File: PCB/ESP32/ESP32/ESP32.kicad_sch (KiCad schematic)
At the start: 32 parts, among them J1 Camera_Receptacle_THT, J1 Conn_01x02_Pin, J1 USB_B_Micro, J2 Conn_01x02_Socket, SW1 RESET, SW2 BOOT, SW3 LRA Switch, U1 DRV2605LTDGSRQ1, U1 ESP32-S2-SOLO-U-N4, U1 MCP73832T-2ACI/OT

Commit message: Footprints for battery
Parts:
- C1, C2: footprint (none) -> Capacitor_SMD:C_0603_1608Metric_Pad1.08x0.95mm_HandSolder
- D1, D2: footprint (none) -> Diode_SMD:D_0603_1608Metric_Pad1.05x0.95mm_HandSolder
- J2: footprint (none) -> Connector_JST:JST_GH_BM02B-GHS-TBT_1x02-1MP_P1.25mm_Vertical
- JP1, JP2: footprint (none) -> Jumper:SolderJumper-2_P1.3mm_Bridged2Bar_Pad1.0x1.5mm
- R1, R2, R3, R4: footprint (none) -> Resistor_SMD:R_0603_1608Metric_Pad0.98x0.95mm_HandSolder
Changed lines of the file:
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@@
 	(label "D7"
 		(at 102.87 78.74 180)
+		(fields_autoplaced yes)
 		(effects
 			(font
@@
 	(label "SDA"
 		(at 273.05 53.34 270)
+		(fields_autoplaced yes)
 		(effects
 			(font
@@
 	(label "MCLK"
 		(at 306.07 123.19 180)
+		(fields_autoplaced yes)
 		(effects
 			(font
@@
 	(label "D1"
 		(at 306.07 140.97 180)
+		(fields_autoplaced yes)
 		(effects
 			(font
@@
 	(label "D3"
 		(at 105.41 69.85 180)
+		(fields_autoplaced yes)
 		(effects
 			(font
@@
 	(label "Reset"
 		(at 306.07 146.05 180)
+		(fields_autoplaced yes)
 		(effects
 			(font
@@
 	(label "D5"
 		(at 306.07 130.81 180)
+		(fields_autoplaced yes)
 		(effects
 			(font
@@
 	(label "Reset"
 		(at 99.06 41.91 180)
+		(fields_autoplaced yes)
 		(effects
 			(font
@@
 	(label "D7"
 		(at 306.07 125.73 180)
+		(fields_autoplaced yes)
 		(effects
 			(font
@@
 	(label "D4"
 		(at 306.07 133.35 180)
+		(fields_autoplaced yes)
 		(effects
 			(font
@@
 	(label "PWNN"
 		(at 307.34 148.59 180)
+		(fields_autoplaced yes)
 		(effects
 			(font
@@
 	(label "VS"
 		(at 105.41 96.52 180)
+		(fields_autoplaced yes)
 		(effects
 			(font
@@
 	(label "D6"
 		(at 105.41 77.47 180)
+		(fields_autoplaced yes)
 		(effects
 			(font
@@
 	(label "USB_D+"
 		(at 45.72 198.12 0)
+		(fields_autoplaced yes)
 		(effects
 			(font
@@
 	(label "D6"
 		(at 306.07 128.27 180)
+		(fields_autoplaced yes)
 		(effects
 			(font
@@
 	(label "SCL"
 		(at 107.95 81.28 180)
+		(fields_autoplaced yes)
 		(effects
 			(font
@@
 	(label "D4"
 		(at 105.41 72.39 180)
+		(fields_autoplaced yes)
 		(effects
 			(font
@@
 	(label "MCLK"
 		(at 105.41 93.98 180)
+		(fields_autoplaced yes)
 		(effects
 			(font
@@
 	(label "D0"
 		(at 105.41 62.23 180)
+		(fields_autoplaced yes)
 		(effects
 			(font
@@
 	(label "D3"
 		(at 306.07 135.89 180)
+		(fields_autoplaced yes)
 		(effects
 			(font
@@
 	(label "USB_D-"
 		(at 148.59 63.5 0)
+		(fields_autoplaced yes)
 		(effects
 			(font
@@
 	(label "PWNN"
 		(at 102.87 88.9 180)
+		(fields_autoplaced yes)
 		(effects
 			(font
@@
 	(label "D0"
 		(at 306.07 143.51 180)
+		(fields_autoplaced yes)
 		(effects
 			(font
@@
 	(label "D2"
 		(at 306.07 138.43 180)
+		(fields_autoplaced yes)
 		(effects
 			(font
@@
 	(label "USB_D+"
 		(at 148.59 66.04 0)
+		(fields_autoplaced yes)
 		(effects
 			(font
@@
 	(label "SDA"
 		(at 107.95 83.82 180)
+		(fields_autoplaced yes)
 		(effects
 			(font
@@
 	(label "VS"
 		(at 309.88 115.57 180)
+		(fields_autoplaced yes)
 		(effects
 			(font
@@
 	(label "PCLK"
 		(at 104.14 91.44 180)
+		(fields_autoplaced yes)
 		(effects
 			(font
@@
 	(label "USB_D-"
 		(at 45.72 200.66 0)
+		(fields_autoplaced yes)
 		(effects
 			(font
@@
 	(label "D1"
 		(at 105.41 64.77 180)
+		(fields_autoplaced yes)
 		(effects
 			(font
@@
 	(label "HS"
 		(at 308.61 118.11 180)
+		(fields_autoplaced yes)
 		(effects
 			(font
@@
 	(label "PCLK"
 		(at 307.34 120.65 180)
+		(fields_autoplaced yes)
 		(effects
 			(font
@@
 	(label "D2"
 		(at 105.41 67.31 180)
+		(fields_autoplaced yes)
 		(effects
 			(font
@@
 	(label "SCLK"
 		(at 287.02 114.3 180)
+		(fields_autoplaced yes)
 		(effects
 			(font
@@
 	(label "D5"
 		(at 105.41 74.93 180)
+		(fields_autoplaced yes)
 		(effects
 			(font
@@
 	(label "HS"
 		(at 148.59 55.88 0)
+		(fields_autoplaced yes)
 		(effects
 			(font
@@
 	(label "SCL"
 		(at 271.78 46.99 270)
+		(fields_autoplaced yes)
 		(effects
 			(font
@@
 			)
 		)
-		(property "Footprint" ""
+		(property "Footprint" "Jumper:SolderJumper-2_P1.3mm_Bridged2Bar_Pad1.0x1.5mm"
 			(at 161.29 199.39 0)
 			(effects
@@
 			)
 		)
-		(property "Footprint" ""
+		(property "Footprint" "Resistor_SMD:R_0603_1608Metric_Pad0.98x0.95mm_HandSolder"
 			(at 171.45 197.358 90)
 			(effects
@@
 			)
 		)
-		(property "Footprint" ""
+		(property "Footprint" "Capacitor_SMD:C_0603_1608Metric_Pad1.08x0.95mm_HandSolder"
 			(at 191.4652 207.01 0)
 			(effects
@@
 			)
 		)
-		(property "Footprint" ""
+		(property "Footprint" "Diode_SMD:D_0603_1608Metric_Pad1.05x0.95mm_HandSolder"
 			(at 90.17 198.12 0)
 			(effects
@@
 			)
 		)
-		(property "Footprint" ""
+		(property "Footprint" "Jumper:SolderJumper-2_P1.3mm_Bridged2Bar_Pad1.0x1.5mm"
 			(at 54.61 196.85 0)
 			(effects
@@
 			)
 		)
-		(property "Footprint" ""
+		(property "Footprint" "Resistor_SMD:R_0603_1608Metric_Pad0.98x0.95mm_HandSolder"
 			(at 171.45 201.422 90)
 			(effects
@@
 			)
 		)
-		(property "Footprint" ""
+		(property "Footprint" "Resistor_SMD:R_0603_1608Metric_Pad0.98x0.95mm_HandSolder"
 			(at 102.87 207.518 90)
 			(effects
@@
 			)
 		)
-		(property "Footprint" ""
+		(property "Footprint" "Capacitor_SMD:C_0603_1608Metric_Pad1.08x0.95mm_HandSolder"
 			(at 70.8152 207.01 0)
 			(effects
@@
 			)
 		)
-		(property "Footprint" ""
+		(property "Footprint" "Diode_SMD:D_0603_1608Metric_Pad1.05x0.95mm_HandSolder"
 			(at 90.17 205.74 0)
 			(effects
@@
 			)
 		)
-		(property "Footprint" ""
+		(property "Footprint" "Resistor_SMD:R_0603_1608Metric_Pad0.98x0.95mm_HandSolder"
 			(at 102.87 199.898 90)
 			(effects
@@
 			)
 		)
-		(property "Footprint" ""
+		(property "Footprint" "Connector_JST:JST_GH_BM02B-GHS-TBT_1x02-1MP_P1.25mm_Vertical"
 			(at 208.28 186.69 0)
 			(effects

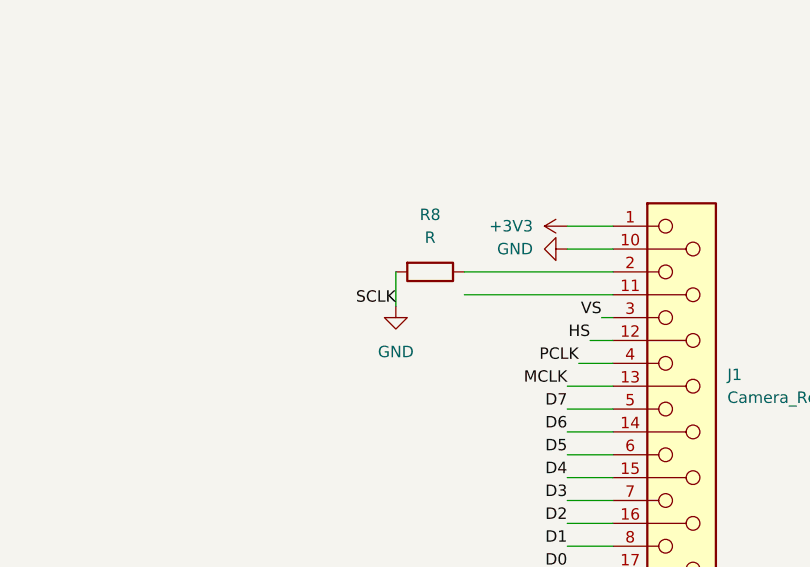
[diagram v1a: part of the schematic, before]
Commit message: Update ESP32.kicad_sch
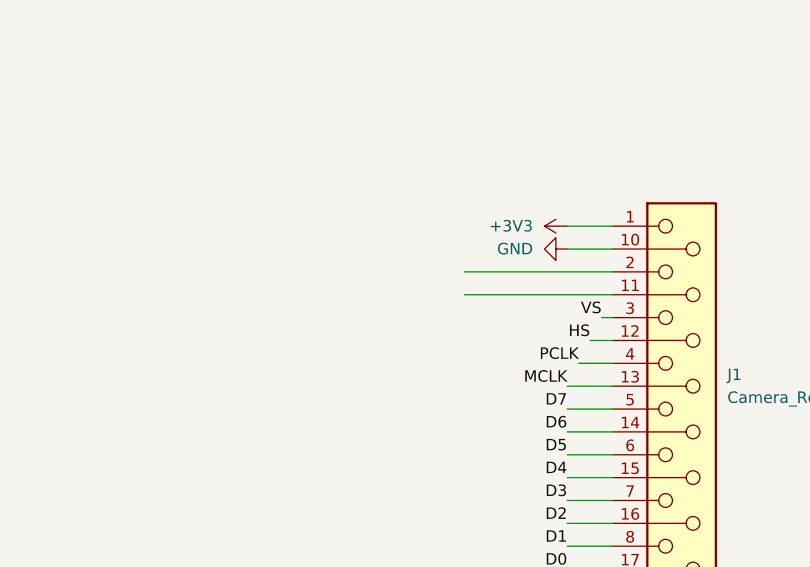
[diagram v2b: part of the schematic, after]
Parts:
- removed R8: R, symbol Device:R
- C1, C2, C5, C6, C7, C8, C9: footprint (none) -> Capacitor_SMD:C_0603_1608Metric
- R1, R2: footprint (none) -> Resistor_SMD:R_0805_2012Metric
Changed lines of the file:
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@@
 	(wire
 		(pts
-			(xy 287.02 110.49) (xy 287.02 114.3)
-		)
-		(stroke
-			(width 0)
-			(type default)
-		)
-	)
-	(wire
-		(pts
 			(xy 313.69 35.56) (xy 313.69 33.02)
 		)
@@
 	(label "D7"
 		(at 102.87 78.74 180)
-		(fields_autoplaced yes)
 		(effects
 			(font
@@
 	(label "SDA"
 		(at 273.05 53.34 270)
-		(fields_autoplaced yes)
 		(effects
 			(font
@@
 	(label "MCLK"
 		(at 306.07 123.19 180)
-		(fields_autoplaced yes)
 		(effects
 			(font
@@
 	(label "D1"
 		(at 306.07 140.97 180)
-		(fields_autoplaced yes)
 		(effects
 			(font
@@
 	(label "D3"
 		(at 105.41 69.85 180)
-		(fields_autoplaced yes)
 		(effects
 			(font
@@
 	(label "Reset"
 		(at 306.07 146.05 180)
-		(fields_autoplaced yes)
 		(effects
 			(font
@@
 	(label "D5"
 		(at 306.07 130.81 180)
-		(fields_autoplaced yes)
 		(effects
 			(font
@@
 	(label "Reset"
 		(at 99.06 41.91 180)
-		(fields_autoplaced yes)
 		(effects
 			(font
@@
 	(label "D7"
 		(at 306.07 125.73 180)
-		(fields_autoplaced yes)
 		(effects
 			(font
@@
 	(label "D4"
 		(at 306.07 133.35 180)
-		(fields_autoplaced yes)
 		(effects
 			(font
@@
 	(label "PWNN"
 		(at 307.34 148.59 180)
-		(fields_autoplaced yes)
 		(effects
 			(font
@@
 	(label "VS"
 		(at 105.41 96.52 180)
-		(fields_autoplaced yes)
 		(effects
 			(font
@@
 	(label "D6"
 		(at 105.41 77.47 180)
-		(fields_autoplaced yes)
 		(effects
 			(font
@@
 	(label "USB_D+"
 		(at 45.72 198.12 0)
-		(fields_autoplaced yes)
 		(effects
 			(font
@@
 	(label "D6"
 		(at 306.07 128.27 180)
-		(fields_autoplaced yes)
 		(effects
 			(font
@@
 	(label "SCL"
 		(at 107.95 81.28 180)
-		(fields_autoplaced yes)
 		(effects
 			(font
@@
 	(label "D4"
 		(at 105.41 72.39 180)
-		(fields_autoplaced yes)
 		(effects
 			(font
@@
 	(label "MCLK"
 		(at 105.41 93.98 180)
-		(fields_autoplaced yes)
 		(effects
 			(font
@@
 	(label "D0"
 		(at 105.41 62.23 180)
-		(fields_autoplaced yes)
 		(effects
 			(font
@@
 	(label "D3"
 		(at 306.07 135.89 180)
-		(fields_autoplaced yes)
 		(effects
 			(font
@@
 	(label "USB_D-"
 		(at 148.59 63.5 0)
-		(fields_autoplaced yes)
 		(effects
 			(font
@@
 	(label "PWNN"
 		(at 102.87 88.9 180)
-		(fields_autoplaced yes)
 		(effects
 			(font
@@
 	(label "D0"
 		(at 306.07 143.51 180)
-		(fields_autoplaced yes)
 		(effects
 			(font
@@
 	(label "D2"
 		(at 306.07 138.43 180)
-		(fields_autoplaced yes)
 		(effects
 			(font
@@
 	(label "USB_D+"
 		(at 148.59 66.04 0)
-		(fields_autoplaced yes)
 		(effects
 			(font
@@
 	(label "SDA"
 		(at 107.95 83.82 180)
-		(fields_autoplaced yes)
 		(effects
 			(font
@@
 	(label "VS"
 		(at 309.88 115.57 180)
-		(fields_autoplaced yes)
 		(effects
 			(font
@@
 	(label "PCLK"
 		(at 104.14 91.44 180)
-		(fields_autoplaced yes)
 		(effects
 			(font
@@
 	(label "USB_D-"
 		(at 45.72 200.66 0)
-		(fields_autoplaced yes)
 		(effects
 			(font
@@
 	(label "D1"
 		(at 105.41 64.77 180)
-		(fields_autoplaced yes)
 		(effects
 			(font
@@
 	(label "HS"
 		(at 308.61 118.11 180)
-		(fields_autoplaced yes)
 		(effects
 			(font
@@
 	(label "PCLK"
 		(at 307.34 120.65 180)
-		(fields_autoplaced yes)
 		(effects
 			(font
@@
 	(label "D2"
 		(at 105.41 67.31 180)
-		(fields_autoplaced yes)
-		(effects
-			(font
-				(size 1.27 1.27)
-			)
-			(justify right bottom)
-		)
-	)
-	(label "SCLK"
-		(at 287.02 114.3 180)
-		(fields_autoplaced yes)
 		(effects
 			(font
@@
 	(label "D5"
 		(at 105.41 74.93 180)
-		(fields_autoplaced yes)
 		(effects
 			(font
@@
 	(label "HS"
 		(at 148.59 55.88 0)
-		(fields_autoplaced yes)
 		(effects
 			(font
@@
 	(label "SCL"
 		(at 271.78 46.99 270)
-		(fields_autoplaced yes)
 		(effects
 			(font
@@
 			)
 		)
-		(property "Footprint" ""
+		(property "Footprint" "Capacitor_SMD:C_0603_1608Metric"
 			(at 166.37 53.34 0)
 			(effects
@@
 			)
 		)
-		(property "Footprint" ""
+		(property "Footprint" "Capacitor_SMD:C_0603_1608Metric"
 			(at 93.98 67.31 0)
 			(effects
@@
 			)
 		)
-		(property "Footprint" ""
+		(property "Footprint" "Capacitor_SMD:C_0603_1608Metric"
 			(at 270.51 38.1 0)
 			(effects
@@
 	)
 	(symbol
-		(lib_id "Device:R")
-		(at 290.83 110.49 270)
-		(unit 1)
-		(exclude_from_sim no)
-		(in_bom yes)
-		(on_board yes)
-		(dnp no)
-		(fields_autoplaced yes)
-		(property "Reference" "R8"
-			(at 290.83 104.14 90)
-			(effects
-				(font
-					(size 1.27 1.27)
-				)
-			)
-		)
-		(property "Value" "R"
-			(at 290.83 106.68 90)
-			(effects
-				(font
-					(size 1.27 1.27)
-				)
-			)
-		)
-		(property "Footprint" ""
-			(at 290.83 108.712 90)
-			(effects
-				(font
-					(size 1.27 1.27)
-				)
-				(hide yes)
-			)
-		)
-		(property "Datasheet" "~"
-			(at 290.83 110.49 0)
-			(effects
-				(font
-					(size 1.27 1.27)
-				)
-				(hide yes)
-			)
-		)
-		(property "Description" "Resistor"
-			(at 290.83 110.49 0)
-			(effects
-				(font
-					(size 1.27 1.27)
-				)
-				(hide yes)
-			)
-		)
-		(pin "1"
-		)
-		(pin "2"
-		)
-		(instances
-			(project ""
-				(path "/f9099a9a-ca12-4d9e-a4e7-b3f085e605c9"
-					(reference "R8")
-					(unit 1)
-				)
-			)
-		)
-	)
-	(symbol
 		(lib_id "power:GND")
 		(at 175.26 212.09 0)
@@
 			)
 		)
-		(property "Footprint" ""
+		(property "Footprint" "Resistor_SMD:R_0805_2012Metric"
 			(at 265.43 55.88 0)
 			(effects
@@
 	)
 	(symbol
-		(lib_id "power:GND")
-		(at 287.02 114.3 0)
-		(unit 1)
-		(exclude_from_sim no)
-		(in_bom yes)
-		(on_board yes)
-		(dnp no)
-		(fields_autoplaced yes)
-		(property "Reference" "#PWR010"
-			(at 287.02 120.65 0)
-			(effects
-				(font
-					(size 1.27 1.27)
-				)
-				(hide yes)
-			)
-		)
-		(property "Value" "GND"
-			(at 287.02 119.38 0)
-			(effects
-				(font
-					(size 1.27 1.27)
-				)
-			)
-		)
-		(property "Footprint" ""
-			(at 287.02 114.3 0)
-			(effects
-				(font
-					(size 1.27 1.27)
-				)
-				(hide yes)
-			)
-		)
-		(property "Datasheet" ""
-			(at 287.02 114.3 0)
-			(effects
-				(font
-					(size 1.27 1.27)
-				)
-				(hide yes)
-			)
-		)
-		(property "Description" "Power symbol creates a global label with name \"GND\" , ground"
-			(at 287.02 114.3 0)
-			(effects
-				(font
-					(size 1.27 1.27)
-				)
-				(hide yes)
-			)
-		)
-		(pin "1"
-		)
-		(instances
-			(project ""
-				(path "/f9099a9a-ca12-4d9e-a4e7-b3f085e605c9"
-					(reference "#PWR010")
-					(unit 1)
-				)
-			)
-		)
-	)
-	(symbol
 		(lib_id "Device:R")
 		(at 171.45 203.2 270)
@@
 			)
 		)
-		(property "Footprint" ""
+		(property "Footprint" "Resistor_SMD:R_0805_2012Metric"
 			(at 259.08 52.07 0)
 			(effects
@@
 			)
 		)
-		(property "Footprint" ""
+		(property "Footprint" "Capacitor_SMD:C_0603_1608Metric"
 			(at 165.1 36.83 0)
 			(effects
@@
 			)
 		)
-		(property "Footprint" ""
+		(property "Footprint" "Capacitor_SMD:C_0603_1608Metric"
 			(at 322.58 49.53 0)
 			(effects
@@
 			)
 		)
-		(property "Footprint" ""
+		(property "Footprint" "Capacitor_SMD:C_0603_1608Metric"
 			(at 88.9 49.53 0)
 			(effects
@@
 			)
 		)
-		(property "Footprint" ""
+		(property "Footprint" "Capacitor_SMD:C_0603_1608Metric"
 			(at 154.94 36.83 0)
 			(effects

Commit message: Schottky Diode footprint
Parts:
- D1: footprint (none) -> Schottky_Diode_Battery:DO-41_STM
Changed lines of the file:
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@@
 	(label "D7"
 		(at 102.87 78.74 180)
+		(fields_autoplaced yes)
 		(effects
 			(font
@@
 	(label "SDA"
 		(at 273.05 53.34 270)
+		(fields_autoplaced yes)
 		(effects
 			(font
@@
 	(label "MCLK"
 		(at 306.07 123.19 180)
+		(fields_autoplaced yes)
 		(effects
 			(font
@@
 	(label "D1"
 		(at 306.07 140.97 180)
+		(fields_autoplaced yes)
 		(effects
 			(font
@@
 	(label "D3"
 		(at 105.41 69.85 180)
+		(fields_autoplaced yes)
 		(effects
 			(font
@@
 	(label "Reset"
 		(at 306.07 146.05 180)
+		(fields_autoplaced yes)
 		(effects
 			(font
@@
 	(label "D5"
 		(at 306.07 130.81 180)
+		(fields_autoplaced yes)
 		(effects
 			(font
@@
 	(label "Reset"
 		(at 99.06 41.91 180)
+		(fields_autoplaced yes)
 		(effects
 			(font
@@
 	(label "D7"
 		(at 306.07 125.73 180)
+		(fields_autoplaced yes)
 		(effects
 			(font
@@
 	(label "D4"
 		(at 306.07 133.35 180)
+		(fields_autoplaced yes)
 		(effects
 			(font
@@
 	(label "PWNN"
 		(at 307.34 148.59 180)
+		(fields_autoplaced yes)
 		(effects
 			(font
@@
 	(label "VS"
 		(at 105.41 96.52 180)
+		(fields_autoplaced yes)
 		(effects
 			(font
@@
 	(label "D6"
 		(at 105.41 77.47 180)
+		(fields_autoplaced yes)
 		(effects
 			(font
@@
 	(label "USB_D+"
 		(at 45.72 198.12 0)
+		(fields_autoplaced yes)
 		(effects
 			(font
@@
 	(label "D6"
 		(at 306.07 128.27 180)
+		(fields_autoplaced yes)
 		(effects
 			(font
@@
 	(label "SCL"
 		(at 107.95 81.28 180)
+		(fields_autoplaced yes)
 		(effects
 			(font
@@
 	(label "D4"
 		(at 105.41 72.39 180)
+		(fields_autoplaced yes)
 		(effects
 			(font
@@
 	(label "MCLK"
 		(at 105.41 93.98 180)
+		(fields_autoplaced yes)
 		(effects
 			(font
@@
 	(label "D0"
 		(at 105.41 62.23 180)
+		(fields_autoplaced yes)
 		(effects
 			(font
@@
 	(label "D3"
 		(at 306.07 135.89 180)
+		(fields_autoplaced yes)
 		(effects
 			(font
@@
 	(label "USB_D-"
 		(at 148.59 63.5 0)
+		(fields_autoplaced yes)
 		(effects
 			(font
@@
 	(label "PWNN"
 		(at 102.87 88.9 180)
+		(fields_autoplaced yes)
 		(effects
 			(font
@@
 	(label "D0"
 		(at 306.07 143.51 180)
+		(fields_autoplaced yes)
 		(effects
 			(font
@@
 	(label "D2"
 		(at 306.07 138.43 180)
+		(fields_autoplaced yes)
 		(effects
 			(font
@@
 	(label "USB_D+"
 		(at 148.59 66.04 0)
+		(fields_autoplaced yes)
 		(effects
 			(font
@@
 	(label "SDA"
 		(at 107.95 83.82 180)
+		(fields_autoplaced yes)
 		(effects
 			(font
@@
 	(label "VS"
 		(at 309.88 115.57 180)
+		(fields_autoplaced yes)
 		(effects
 			(font
@@
 	(label "PCLK"
 		(at 104.14 91.44 180)
+		(fields_autoplaced yes)
 		(effects
 			(font
@@
 	(label "USB_D-"
 		(at 45.72 200.66 0)
+		(fields_autoplaced yes)
 		(effects
 			(font
@@
 	(label "D1"
 		(at 105.41 64.77 180)
+		(fields_autoplaced yes)
 		(effects
 			(font
@@
 	(label "HS"
 		(at 308.61 118.11 180)
+		(fields_autoplaced yes)
 		(effects
 			(font
@@
 	(label "PCLK"
 		(at 307.34 120.65 180)
+		(fields_autoplaced yes)
 		(effects
 			(font
@@
 	(label "D2"
 		(at 105.41 67.31 180)
+		(fields_autoplaced yes)
 		(effects
 			(font
@@
 	(label "D5"
 		(at 105.41 74.93 180)
+		(fields_autoplaced yes)
 		(effects
 			(font
@@
 	(label "HS"
 		(at 148.59 55.88 0)
+		(fields_autoplaced yes)
 		(effects
 			(font
@@
 	(label "SCL"
 		(at 271.78 46.99 270)
+		(fields_autoplaced yes)
 		(effects
 			(font
@@
 			)
 		)
-		(property "Footprint" ""
+		(property "Footprint" "Schottky_Diode_Battery:DO-41_STM"
 			(at 195.58 186.69 0)
 			(effects
